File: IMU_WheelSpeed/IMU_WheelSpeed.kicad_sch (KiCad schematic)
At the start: 24 parts, among them J1 Conn_01x06_Socket, J2 CAN_IN, J3 Conn_01x03_Socket, J4 CAN_OUT, J5 PWR_IN, J6 PWR_OUT, J7 Conn_01x03_Socket, U1 PeripheralSOM, U4 TPS71518__SC70

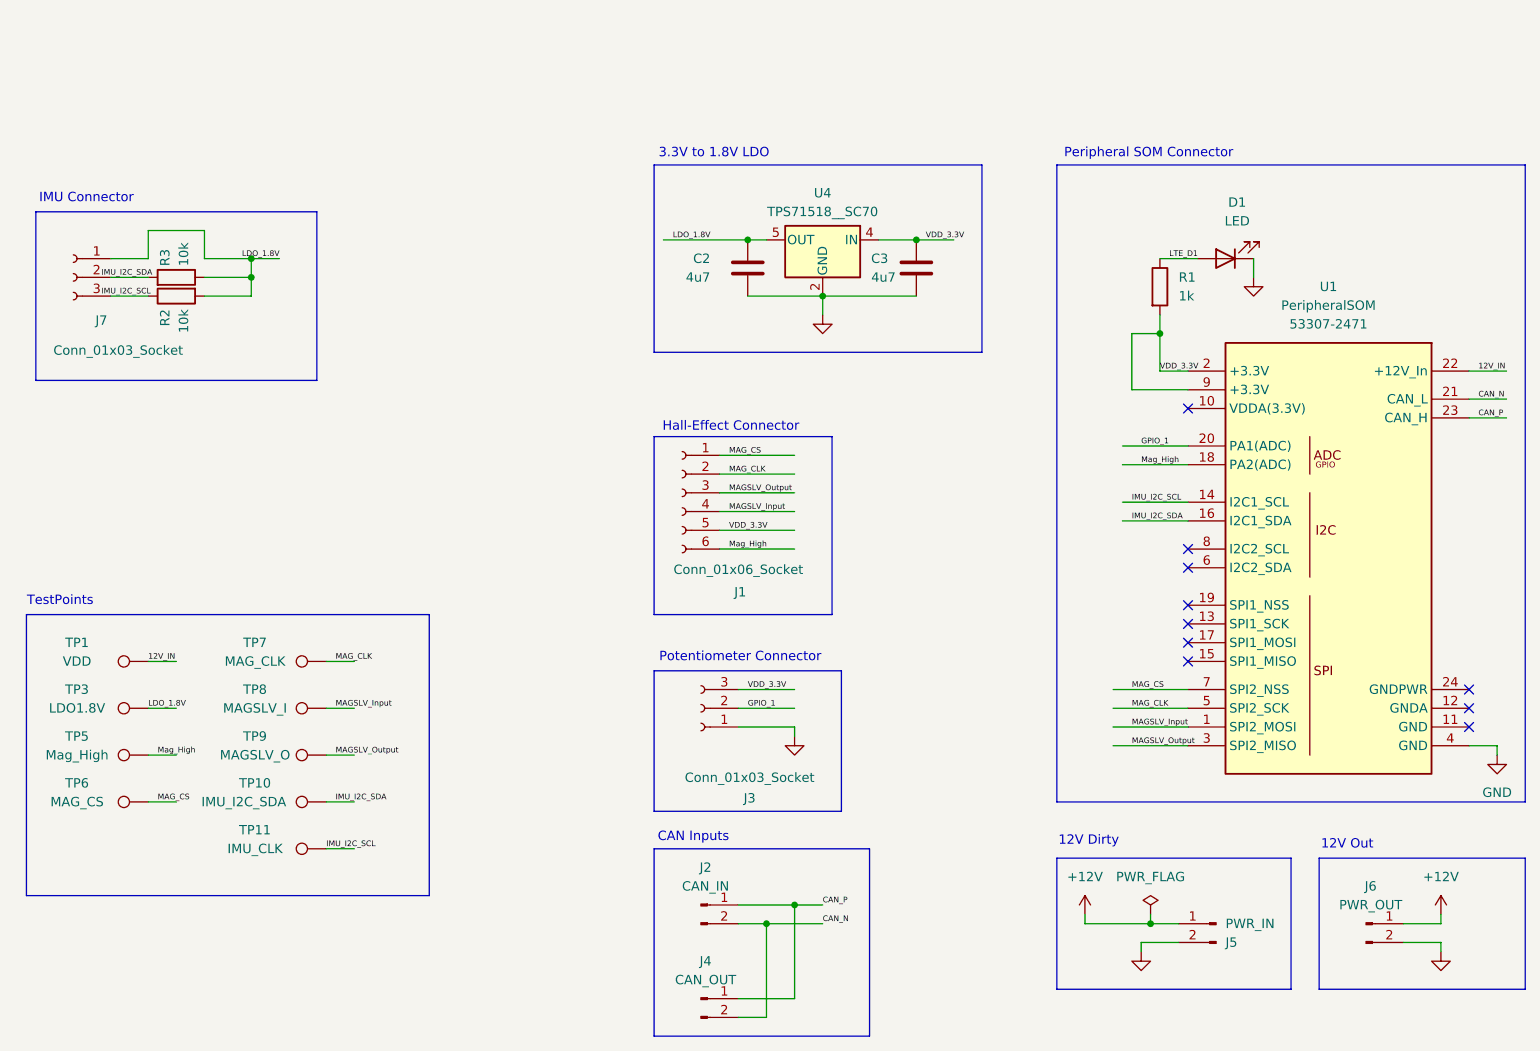
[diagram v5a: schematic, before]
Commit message: Switched LDO Caps
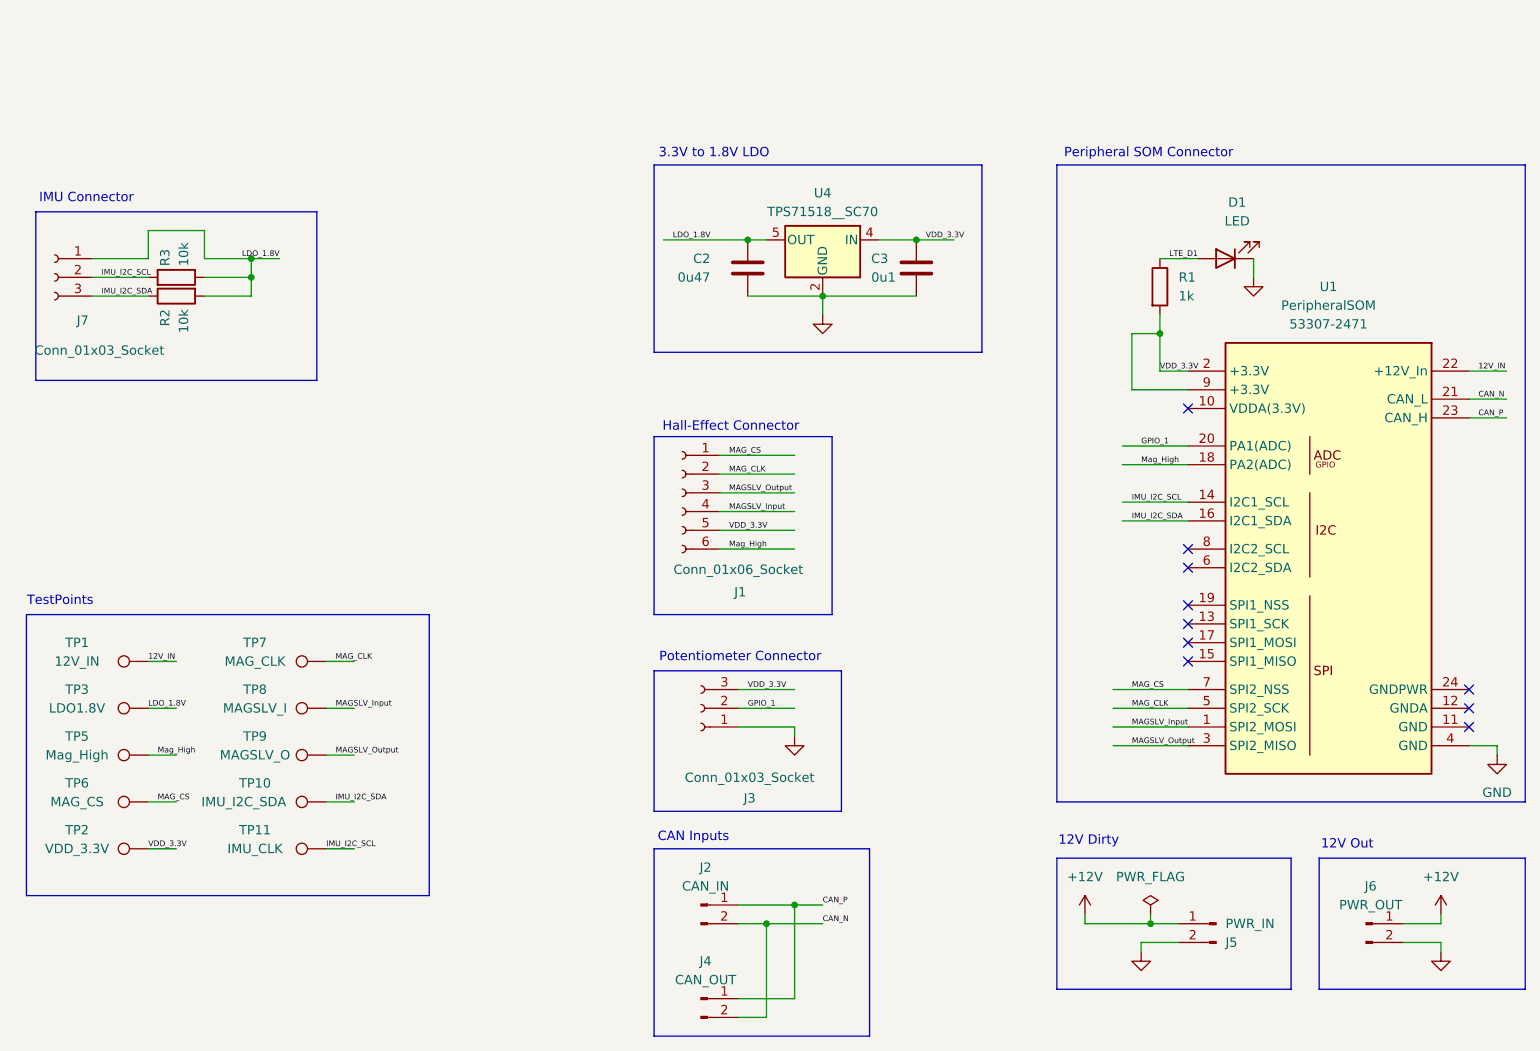
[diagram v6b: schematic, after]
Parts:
- added TP2: VDD_3.3V, TestPoint:TestPoint_THTPad_D2.0mm_Drill1.0mm, symbol Connector:TestPoint
- C2: value 4u7 -> 0u47
- C3: value 4u7 -> 0u1
- TP1: value VDD -> 12V_IN; footprint TestPoint:TestPoint_THTPad_D3.0mm_Drill1.5mm -> TestPoint:TestPoint_THTPad_D2.0mm_Drill1.0mm
- TP10, TP11, TP3, TP5, TP6, TP7, TP8, TP9: footprint TestPoint:TestPoint_THTPad_D3.0mm_Drill1.5mm -> TestPoint:TestPoint_THTPad_D2.0mm_Drill1.0mm
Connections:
- net IMU_I2C_SCL: now also J7.2 (Pin_2), R3.2
- net IMU_I2C_SDA: now also J7.3 (Pin_3), R2.1
- net VDD_3.3V: now also TP2.1
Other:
- moved on the sheet: J7
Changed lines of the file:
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@@
 	(wire
 		(pts
-			(xy 68.58 57.15) (xy 63.5 57.15)
+			(xy 68.58 57.15) (xy 60.96 57.15)
 		)
 		(stroke
@@
 	(wire
 		(pts
-			(xy 68.58 59.69) (xy 63.5 59.69)
+			(xy 68.58 59.69) (xy 60.96 59.69)
 		)
 		(stroke
@@
 	(wire
 		(pts
+			(xy 68.58 137.16) (xy 72.39 137.16)
+		)
+		(stroke
+			(width 0)
+			(type default)
+		)
+	)
+	(wire
+		(pts
 			(xy 160.02 62.23) (xy 160.02 64.77)
 		)
@@
 	(wire
 		(pts
-			(xy 68.58 62.23) (xy 63.5 62.23)
+			(xy 68.58 62.23) (xy 60.96 62.23)
 		)
 		(stroke
@@
 	)
 	(label "IMU_I2C_SCL"
-		(at 62.23 62.23 0)
+		(at 62.23 59.69 0)
 		(fields_autoplaced yes)
 		(effects
@@
 	)
 	(label "IMU_I2C_SDA"
-		(at 62.23 59.69 0)
+		(at 62.23 62.23 0)
 		(fields_autoplaced yes)
 		(effects
@@
 		)
 	)
+	(label "VDD_3.3V"
+		(at 68.58 137.16 0)
+		(fields_autoplaced yes)
+		(effects
+			(font
+				(size 0.762 0.762)
+			)
+			(justify left bottom)
+		)
+	)
 	(label "MAGSLV_Output"
 		(at 201.93 123.19 0)
@@
 			)
 		)
-		(property "Footprint" "TestPoint:TestPoint_THTPad_D3.0mm_Drill1.5mm"
+		(property "Footprint" "TestPoint:TestPoint_THTPad_D2.0mm_Drill1.0mm"
 			(at 92.71 129.54 0)
 			(effects
@@
 			)
 		)
-		(property "Value" "VDD"
+		(property "Value" "12V_IN"
 			(at 58.928 111.76 90)
 			(effects
@@
 			)
 		)
-		(property "Footprint" "TestPoint:TestPoint_THTPad_D3.0mm_Drill1.5mm"
+		(property "Footprint" "TestPoint:TestPoint_THTPad_D2.0mm_Drill1.0mm"
 			(at 68.58 116.84 0)
 			(effects
@@
 			)
 		)
-		(property "Footprint" "TestPoint:TestPoint_THTPad_D3.0mm_Drill1.5mm"
+		(property "Footprint" "TestPoint:TestPoint_THTPad_D2.0mm_Drill1.0mm"
 			(at 92.71 116.84 0)
 			(effects
@@
 	(symbol
 		(lib_id "Connector:Conn_01x03_Socket")
-		(at 58.42 59.69 0)
+		(at 55.88 59.69 0)
 		(mirror y)
 		(unit 1)
@@
 		(dnp no)
 		(property "Reference" "J7"
-			(at 62.23 65.532 0)
+			(at 59.69 65.532 0)
 			(effects
 				(font
@@
 		)
 		(property "Value" "Conn_01x03_Socket"
-			(at 64.516 69.596 0)
+			(at 61.976 69.596 0)
 			(effects
 				(font
@@
 		)
 		(property "Footprint" "UTSVT_Connectors:Molex_MicroFit3.0_1x3xP3.00mm_PolarizingPeg_Vertical"
-			(at 58.42 59.69 0)
+			(at 55.88 59.69 0)
 			(effects
 				(font
@@
 		)
 		(property "Datasheet" "~"
-			(at 58.42 59.69 0)
+			(at 55.88 59.69 0)
 			(effects
 				(font
@@
 		)
 		(property "Description" "Generic connector, single row, 01x03, script generated"
-			(at 58.42 59.69 0)
+			(at 55.88 59.69 0)
 			(effects
 				(font
@@
 			)
 		)
-		(property "Footprint" "TestPoint:TestPoint_THTPad_D3.0mm_Drill1.5mm"
+		(property "Footprint" "TestPoint:TestPoint_THTPad_D2.0mm_Drill1.0mm"
 			(at 68.58 129.54 0)
 			(effects
@@
 	(symbol
 		(lib_id "Connector:TestPoint")
+		(at 68.58 137.16 90)
+		(mirror x)
+		(unit 1)
+		(exclude_from_sim no)
+		(in_bom yes)
+		(on_board yes)
+		(dnp no)
+		(property "Reference" "TP2"
+			(at 58.928 134.62 90)
+			(effects
+				(font
+					(size 1.27 1.27)
+				)
+			)
+		)
+		(property "Value" "VDD_3.3V"
+			(at 58.928 137.16 90)
+			(effects
+				(font
+					(size 1.27 1.27)
+				)
+			)
+		)
+		(property "Footprint" "TestPoint:TestPoint_THTPad_D2.0mm_Drill1.0mm"
+			(at 68.58 142.24 0)
+			(effects
+				(font
+					(size 1.27 1.27)
+				)
+				(hide yes)
+			)
+		)
+		(property "Datasheet" "~"
+			(at 68.58 142.24 0)
+			(effects
+				(font
+					(size 1.27 1.27)
+				)
+				(hide yes)
+			)
+		)
+		(property "Description" "test point"
+			(at 68.58 137.16 0)
+			(effects
+				(font
+					(size 1.27 1.27)
+				)
+				(hide yes)
+			)
+		)
+		(pin "1"
+		)
+		(instances
+			(project "IMU_WheelSpeed"
+				(path "/14f79712-0700-402e-8c34-7a7e829c8748"
+					(reference "TP2")
+					(unit 1)
+				)
+			)
+		)
+	)
+	(symbol
+		(lib_id "Connector:TestPoint")
 		(at 68.58 130.81 90)
 		(mirror x)
@@
 			)
 		)
-		(property "Footprint" "TestPoint:TestPoint_THTPad_D3.0mm_Drill1.5mm"
+		(property "Footprint" "TestPoint:TestPoint_THTPad_D2.0mm_Drill1.0mm"
 			(at 68.58 135.89 0)
 			(effects
@@
 			)
 		)
-		(property "Footprint" "TestPoint:TestPoint_THTPad_D3.0mm_Drill1.5mm"
+		(property "Footprint" "TestPoint:TestPoint_THTPad_D2.0mm_Drill1.0mm"
 			(at 92.71 123.19 0)
 			(effects
@@
 			)
 		)
-		(property "Footprint" "TestPoint:TestPoint_THTPad_D3.0mm_Drill1.5mm"
+		(property "Footprint" "TestPoint:TestPoint_THTPad_D2.0mm_Drill1.0mm"
 			(at 92.71 142.24 0)
 			(effects
@@
 			)
 		)
-		(property "Value" "4u7"
+		(property "Value" "0u47"
 			(at 144.78 59.6899 0)
 			(effects
@@
 			)
 		)
-		(property "Value" "4u7"
+		(property "Value" "0u1"
 			(at 169.926 59.69 0)
 			(effects
@@
 			)
 		)
-		(property "Footprint" "TestPoint:TestPoint_THTPad_D3.0mm_Drill1.5mm"
+		(property "Footprint" "TestPoint:TestPoint_THTPad_D2.0mm_Drill1.0mm"
 			(at 68.58 123.19 0)
 			(effects
@@
 			)
 		)
-		(property "Footprint" "TestPoint:TestPoint_THTPad_D3.0mm_Drill1.5mm"
+		(property "Footprint" "TestPoint:TestPoint_THTPad_D2.0mm_Drill1.0mm"
 			(at 92.71 135.89 0)
 			(effects

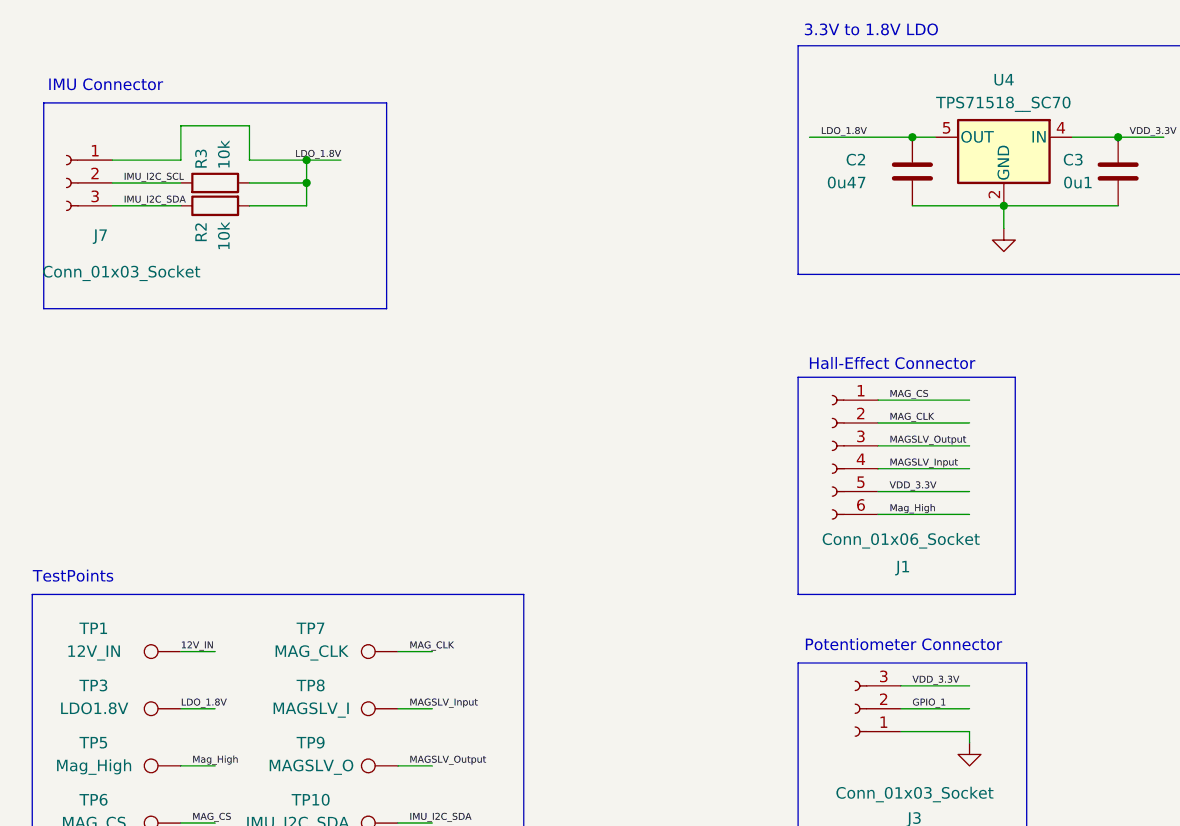
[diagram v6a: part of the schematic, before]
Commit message: Approved Connectors and gnd connected
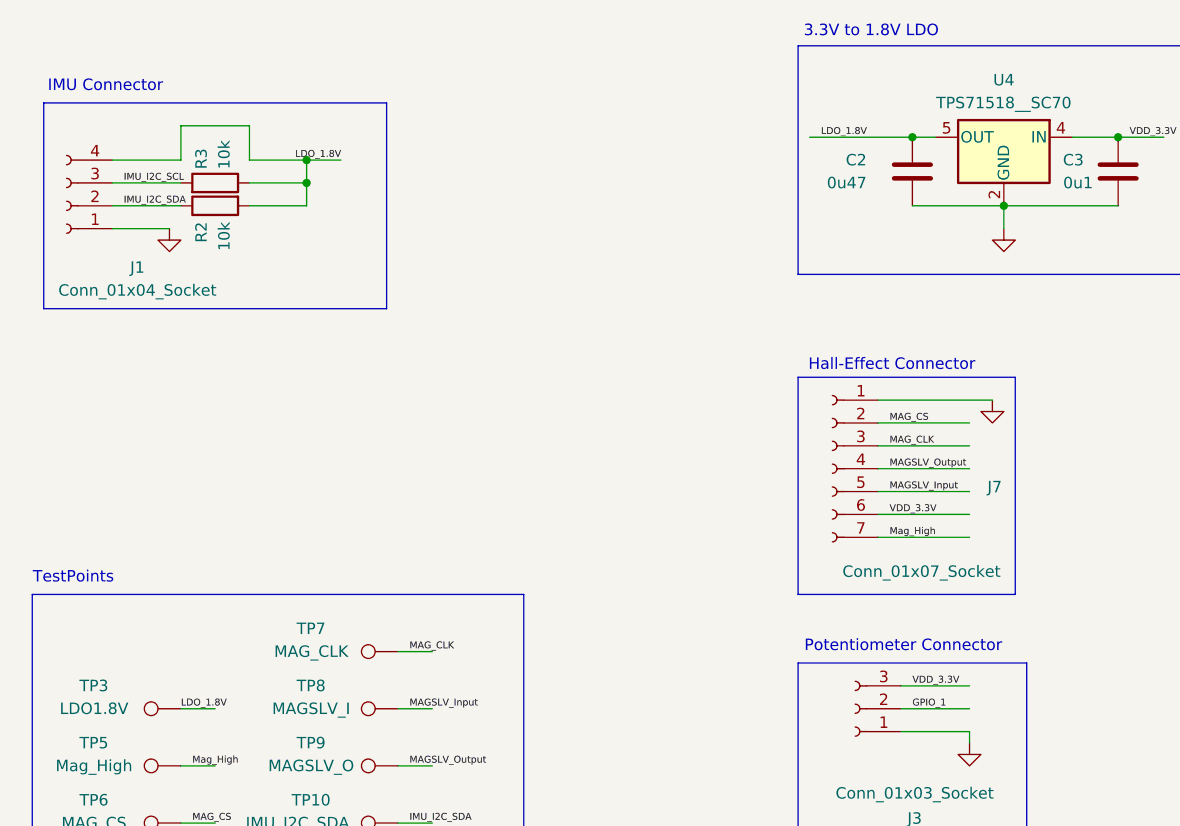
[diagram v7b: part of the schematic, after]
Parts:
- removed J1: Conn_01x06_Socket, UTSVT_Connectors:Molex_MicroFit_01x06_Horizontal, symbol Connector:Conn_01x06_Socket
- removed J7: Conn_01x03_Socket, UTSVT_Connectors:Molex_MicroFit3.0_1x3xP3.00mm_PolarizingPeg_Vertical, symbol Connector:Conn_01x03_Socket
- removed TP1: 12V_IN, TestPoint:TestPoint_THTPad_D2.0mm_Drill1.0mm, symbol Connector:TestPoint
- added J1: Conn_01x04_Socket, Connector_Molex:Molex_Nano-Fit_105309-xx04_1x04_P2.50mm_Vertical, symbol Connector:Conn_01x04_Socket
- added J7: Conn_01x07_Socket, Connector_Molex:Molex_Nano-Fit_105313-xx07_1x07_P2.50mm_Horizontal, symbol Connector:Conn_01x07_Socket
- J3: footprint UTSVT_Connectors:Molex_MicroFit3.0_1x3xP3.00mm_PolarizingPeg_Vertical -> Connector_Molex:Molex_Nano-Fit_105309-xx03_1x03_P2.50mm_Vertical
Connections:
- net GND: now also J1.1 (Pin_1), J7.1 (Pin_1)
- net IMU_I2C_SCL: now also J1.3 (Pin_3)
- net IMU_I2C_SDA: now also J1.2 (Pin_2)
- net LDO_1.8V: now also J1.4 (Pin_4)
- net MAGSLV_Input: now also J7.5 (Pin_5)
- net MAGSLV_Output: now also J7.4 (Pin_4)
- net MAG_CLK: now also J7.3 (Pin_3)
- net MAG_CS: now also J7.2 (Pin_2)
- net Mag_High: now also J7.7 (Pin_7)
- net VDD_3.3V: now also J7.6 (Pin_6)

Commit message: made cuter and added silkscreens
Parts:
- removed J7: Conn_01x07_Socket, Connector_Molex:Molex_Nano-Fit_105313-xx07_1x07_P2.50mm_Horizontal, symbol Connector:Conn_01x07_Socket
- removed TP5: Mag_High, TestPoint:TestPoint_THTPad_D2.0mm_Drill1.0mm, symbol Connector:TestPoint
- added J7: Conn_01x06_Socket, Connector_Molex:Molex_Nano-Fit_105309-xx06_1x06_P2.50mm_Vertical, symbol Connector:Conn_01x06_Socket
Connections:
- net 12V_IN is gone; now on net +12V: U1.22 (+12V_In)
- net GND: now also J7.6 (Pin_6)
- net MAGSLV_Input: now also J7.2 (Pin_2)
- net MAGSLV_Output: now also J7.3 (Pin_3)
- net MAG_CLK: now also J7.4 (Pin_4)
- net MAG_CS: now also J7.5 (Pin_5)
- net VDD_3.3V: now also J7.1 (Pin_1)
- net Mag_High: no longer names the net of U1.18 (PA2(ADC))
- no-connect marks 10 -> 11
